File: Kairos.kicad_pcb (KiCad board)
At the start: 2 copper layers, 285 x 94.6 mm, 134 parts, among them Q1 NSS40301MZ4T1G, SW1 SW_RST1, U1 ATMEGA32U2-AU, Y1 Crystal_GND24

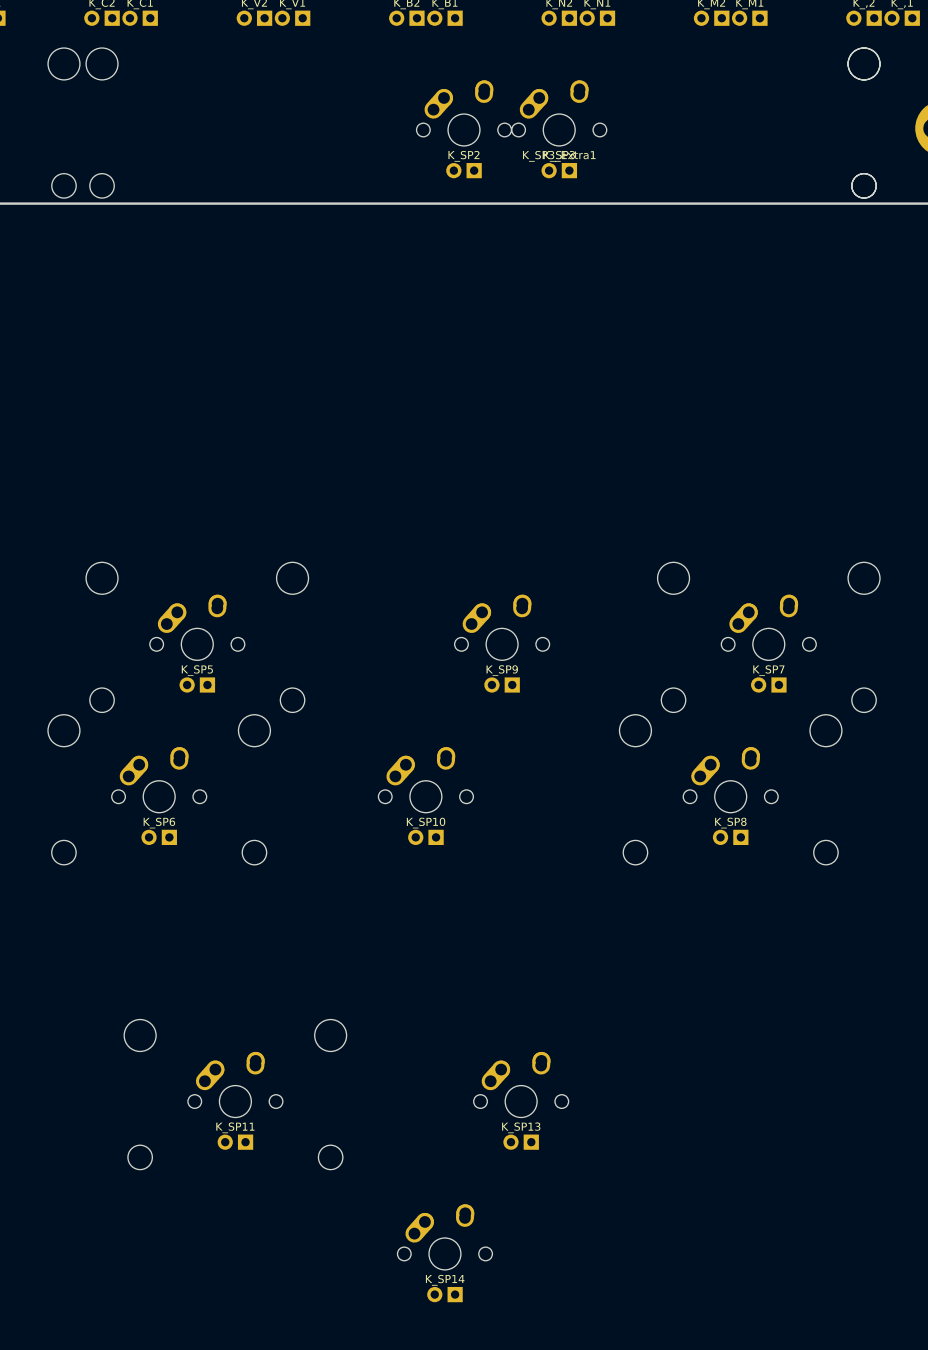
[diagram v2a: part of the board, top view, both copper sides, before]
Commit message: Remove SP14, clean up PCB
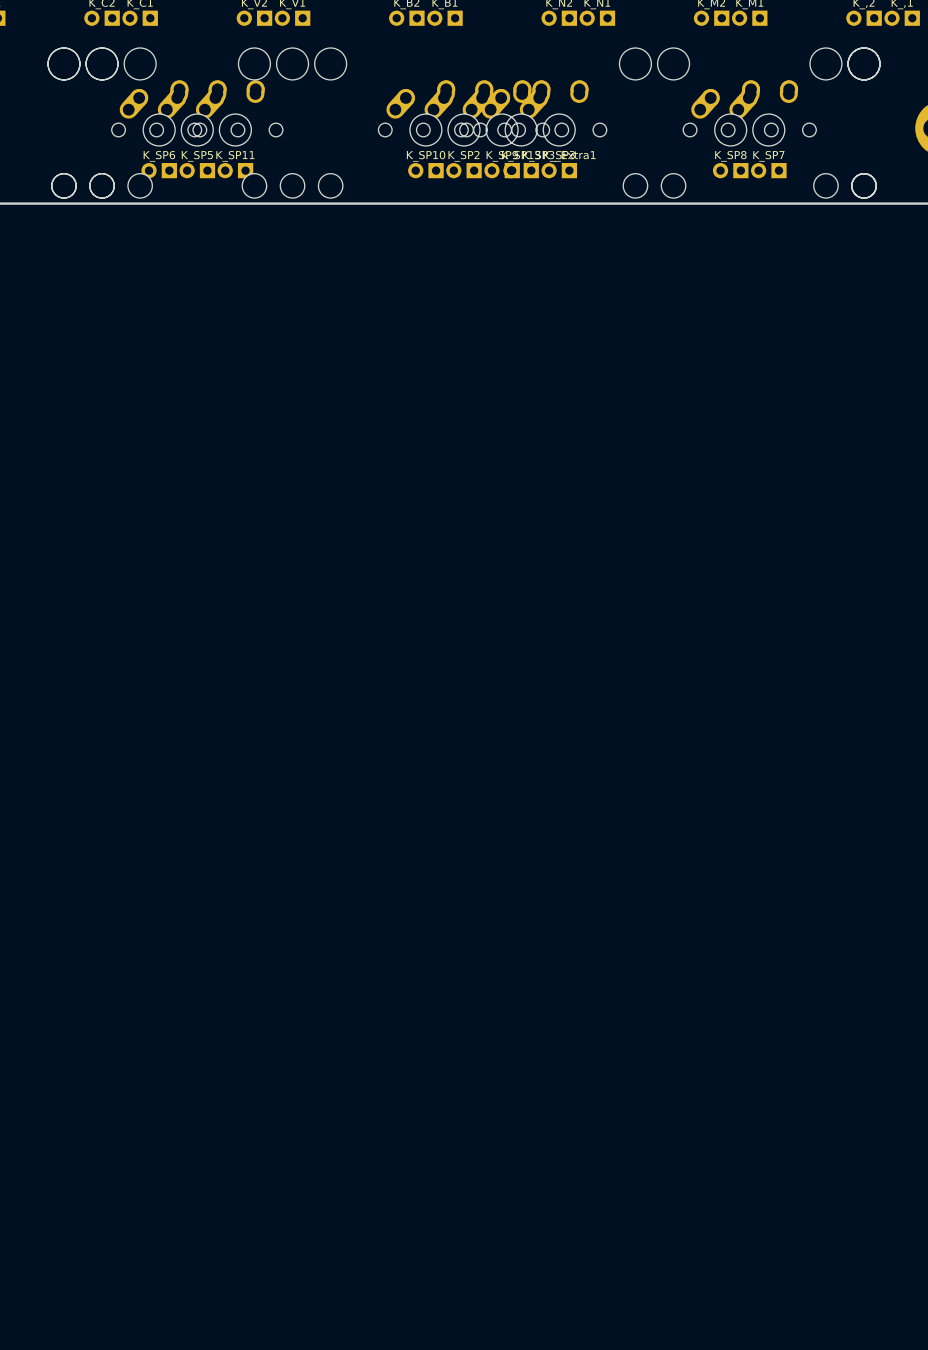
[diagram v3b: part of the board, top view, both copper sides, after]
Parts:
- removed K_SP14: MX-1U, MX_Alps_Hybrid:MX-1U
- moved K_SP11 121.4 mm to (107.2, 107.2)
- moved K_SP13 121.4 mm to (142.9, 107.2)
- moved K_SP10 83.3 mm to (131.0, 107.2)
- moved K_SP6 83.3 mm to (97.6, 107.2)
- moved K_SP8 83.3 mm to (169.1, 107.2)
- moved K_SP5 64.3 mm to (102.4, 107.2)
- moved K_SP7 64.3 mm to (173.8, 107.2)
- moved K_SP9 64.3 mm to (140.5, 107.2)
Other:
- board text removed: "Addons to RM7 and RM12"
- board text removed: "Split 6 Combined with 2.75 from Var2, Shares 2.75 from Var1 for 2.25"
- board text removed: "Split 6 Combined with Split 6.25 Var1"
- board text removed: "Split 6.25 Variant 1"
- board text removed: "Split 6.25 Variant 2"
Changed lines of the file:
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@@
 (kicad_pcb (version 4) (host pcbnew 4.0.6)
   (general
-    (links 573)
-    (no_connects 307)
+    (links 567)
+    (no_connects 303)
     (area 0 0 0 0)
     (thickness 1.6)
-    (drawings 7)
+    (drawings 2)
     (tracks 278)
     (zones 0)
-    (modules 134)
+    (modules 133)
     (nets 189)
   )
@@
   )
   (module MX_Alps_Hybrid:MX-1.25U (layer F.Cu)
-    (at 140.49375 171.45)
+    (at 140.49375 107.15625)
     (fp_text reference K_SP9 (at 0 3.175) (layer F.SilkS)
       (effects (font (size 1 1) (thickness 0.15)))
@@
   )
   (module MX_Alps_Hybrid:MX-1.25U (layer F.Cu)
-    (at 130.96875 190.5)
+    (at 130.96875 107.15625)
     (fp_text reference K_SP10 (at 0 3.175) (layer F.SilkS)
       (effects (font (size 1 1) (thickness 0.15)))
@@
   )
   (module MX_Alps_Hybrid:MX-1U (layer F.Cu)
-    (at 133.35 247.65)
-    (fp_text reference K_SP14 (at 0 3.175) (layer F.SilkS)
-      (effects (font (size 1 1) (thickness 0.15)))
-    )
-    (fp_text value MX-1U (at 0 -7.9375) (layer Dwgs.User)
-      (effects (font (size 1 1) (thickness 0.15)))
-    )
-    (fp_line (start 5 -7) (end 7 -7) (layer Dwgs.User) (width 0.15))
-    (fp_line (start 7 -7) (end 7 -5) (layer Dwgs.User) (width 0.15))
-    (fp_line (start 5 7) (end 7 7) (layer Dwgs.User) (width 0.15))
-    (fp_line (start 7 7) (end 7 5) (layer Dwgs.User) (width 0.15))
-    (fp_line (start -7 5) (end -7 7) (layer Dwgs.User) (width 0.15))
-    (fp_line (start -7 7) (end -5 7) (layer Dwgs.User) (width 0.15))
-    (fp_line (start -5 -7) (end -7 -7) (layer Dwgs.User) (width 0.15))
-    (fp_line (start -7 -7) (end -7 -5) (layer Dwgs.User) (width 0.15))
-    (fp_line (start -9.525 -9.525) (end 9.525 -9.525) (layer Dwgs.User) (width 0.15))
-    (fp_line (start 9.525 -9.525) (end 9.525 9.525) (layer Dwgs.User) (width 0.15))
-    (fp_line (start 9.525 9.525) (end -9.525 9.525) (layer Dwgs.User) (width 0.15))
-    (fp_line (start -9.525 9.525) (end -9.525 -9.525) (layer Dwgs.User) (width 0.15))
-    (pad 2 thru_hole oval (at 2.5 -4.5 86.0548) (size 2.831378 2.25) (drill 1.47 (offset 0.290689 0)) (layers *.Cu *.Mask)
-      (net 74 COL4))
-    (pad 2 thru_hole circle (at 2.54 -5.08) (size 2.25 2.25) (drill 1.47) (layers *.Cu *.Mask)
-      (net 74 COL4))
-    (pad 1 thru_hole oval (at -3.81 -2.54 48.09963212) (size 4.211556 2.25) (drill 1.47 (offset 0.980778 0)) (layers *.Cu *.Mask)
-      (net 35 ROW8))
-    (pad "" np_thru_hole circle (at 0 0) (size 3.9878 3.9878) (drill 3.9878) (layers *.Cu *.Mask))
-    (pad 1 thru_hole circle (at -2.5 -4) (size 2.25 2.25) (drill 1.47) (layers *.Cu *.Mask)
-      (net 35 ROW8))
-    (pad 3 thru_hole circle (at -1.27 5.08) (size 1.905 1.905) (drill 1.04) (layers *.Cu *.Mask)
-      (net 187 "Net-(K_SP10-Pad3)"))
-    (pad 4 thru_hole rect (at 1.27 5.08) (size 1.905 1.905) (drill 1.04) (layers *.Cu *.Mask)
-      (net 2 LEDGND))
-    (pad "" np_thru_hole circle (at -5.08 0 48.0996) (size 1.7018 1.7018) (drill 1.7018) (layers *.Cu *.Mask))
-    (pad "" np_thru_hole circle (at 5.08 0 48.0996) (size 1.7018 1.7018) (drill 1.7018) (layers *.Cu *.Mask))
-  )
-  (module MX_Alps_Hybrid:MX-1U (layer F.Cu)
-    (at 142.875 228.6)
+    (at 142.875 107.15625)
     (fp_text reference K_SP13 (at 0 3.175) (layer F.SilkS)
       (effects (font (size 1 1) (thickness 0.15)))
@@
   )
   (module MX_Alps_Hybrid:MX-2.75U-ReversedStabilizer (layer F.Cu)
-    (at 102.39375 171.45)
+    (at 102.39375 107.15625)
     (fp_text reference K_SP5 (at 0 3.175) (layer F.SilkS)
       (effects (font (size 1 1) (thickness 0.15)))
@@
   )
   (module MX_Alps_Hybrid:MX-2.25U-ReversedStabilizer (layer F.Cu)
-    (at 97.63125 190.5)
+    (at 97.63125 107.15625)
     (fp_text reference K_SP6 (at 0 3.175) (layer F.SilkS)
       (effects (font (size 1 1) (thickness 0.15)))
@@
   )
   (module MX_Alps_Hybrid:MX-2.25U-ReversedStabilizer (layer F.Cu)
-    (at 173.83125 171.45)
+    (at 173.83125 107.15625)
     (fp_text reference K_SP7 (at 0 3.175) (layer F.SilkS)
       (effects (font (size 1 1) (thickness 0.15)))
@@
   )
   (module MX_Alps_Hybrid:MX-2.75U-ReversedStabilizer (layer F.Cu)
-    (at 169.06875 190.5)
+    (at 169.06875 107.15625)
     (fp_text reference K_SP8 (at 0 3.175) (layer F.SilkS)
       (effects (font (size 1 1) (thickness 0.15)))
@@
   )
   (module MX_Alps_Hybrid:MX-2.75U-ReversedStabilizer (layer F.Cu)
-    (at 107.15625 228.6)
+    (at 107.15625 107.15625)
     (fp_text reference K_SP11 (at 0 3.175) (layer F.SilkS)
       (effects (font (size 1 1) (thickness 0.15)))
@@
     (pad "" np_thru_hole circle (at 11.90625 -8.255) (size 3.9878 3.9878) (drill 3.9878) (layers *.Cu *.Mask))
   )
-  (gr_text "To left and right:\n1.5-1.25-1.5 setups for\napple row (6.5U Space shares SP3)\n" (at 143.66875 285.75) (layer Dwgs.User)
-    (effects (font (size 1.5 1.5) (thickness 0.3)))
-  )
-  (gr_text "Addons to\nRM7 and RM12" (at 256.38125 246.85625) (layer Dwgs.User)
-    (effects (font (size 1.5 1.5) (thickness 0.3)))
-  )
-  (gr_text "Split 6\nCombined with 2.75 from Var2,\nShares 2.75 from Var1 for 2.25\n" (at 164.30625 246.85625) (layer Dwgs.User)
-    (effects (font (size 1.5 1.5) (thickness 0.3)))
-  )
-  (gr_text "Split 6\nCombined with\nSplit 6.25 Var1" (at 162.71875 228.6) (layer Dwgs.User)
-    (effects (font (size 1.5 1.5) (thickness 0.3)))
-  )
-  (gr_text "Split 6.25\nVariant 2\n" (at 204.7875 190.5) (layer Dwgs.User)
-    (effects (font (size 1.5 1.5) (thickness 0.3)))
-  )
-  (gr_text "Split 6.25\nVariant 1" (at 204.7875 170.65625) (layer Dwgs.User)
+  (gr_text 107.15625 (at 237.33125 150.8125) (layer Dwgs.User)
     (effects (font (size 1.5 1.5) (thickness 0.3)))
   )
-  (gr_text 107.15625 (at 237.33125 150.8125) (layer Dwgs.User)
+  (gr_text "To left and right:\n1.5-1.25-1.5 setups for\napple row (6.5U Space shares SP3)\n" (at 143.66875 285.75) (layer Dwgs.User)
     (effects (font (size 1.5 1.5) (thickness 0.3)))
   )

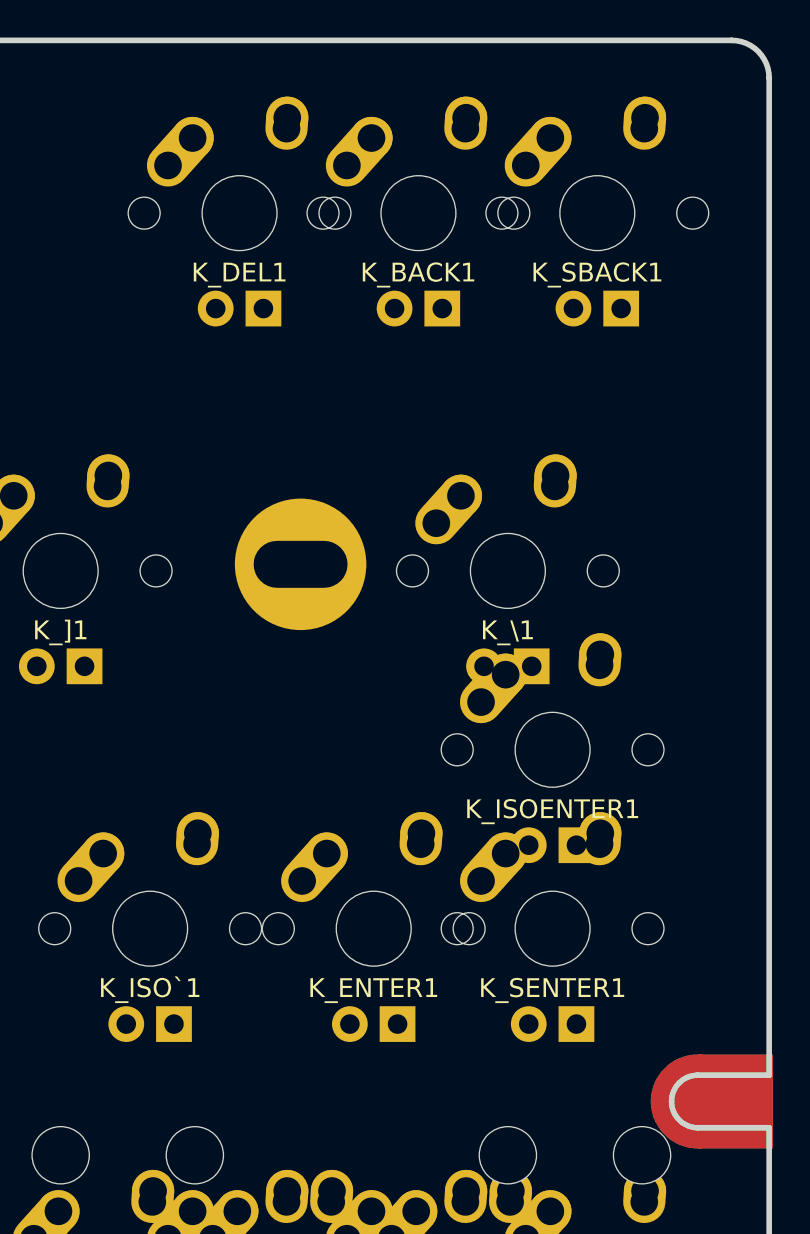
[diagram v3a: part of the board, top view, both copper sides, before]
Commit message: Fix first batch of wrong size footprints
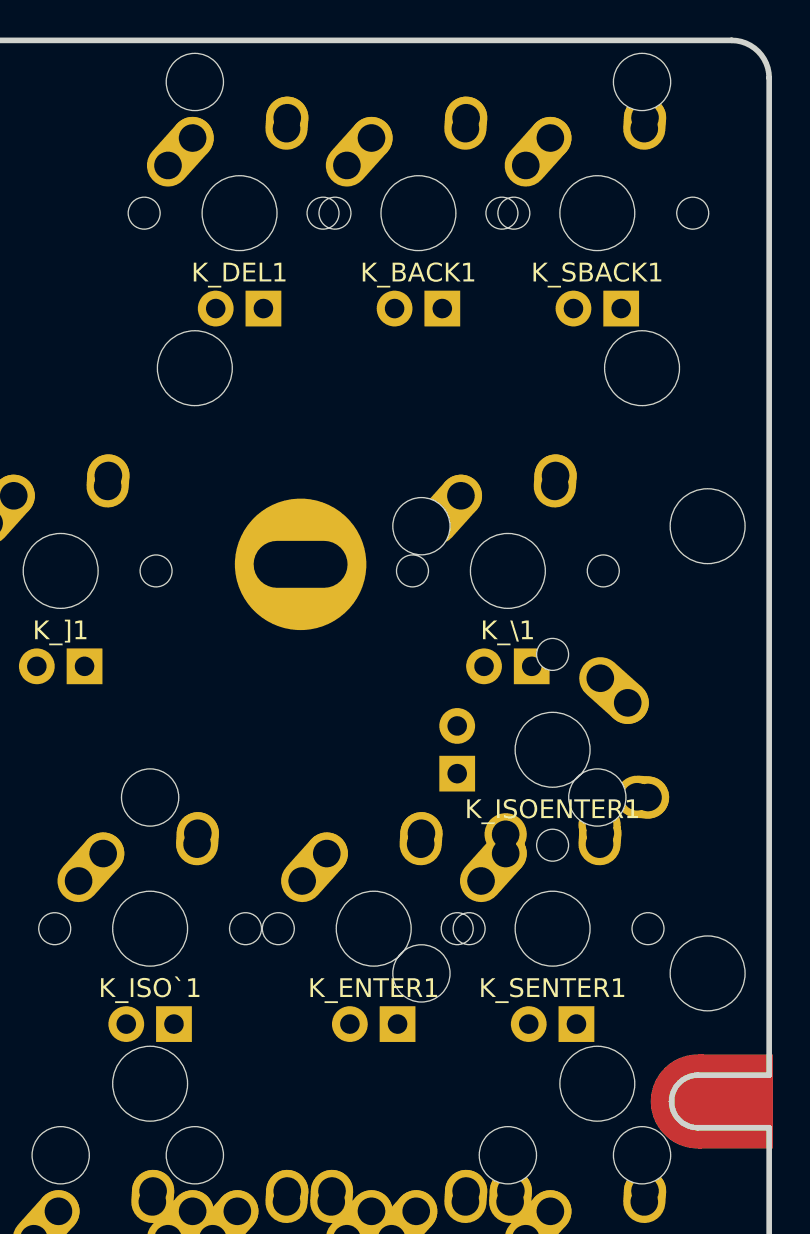
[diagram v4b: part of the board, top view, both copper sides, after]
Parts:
- K_BACK1: footprint MX_Alps_Hybrid:MX-1U -> MX_Alps_Hybrid:MX-2U
- K_CAPS1: footprint MX_Alps_Hybrid:MX-1U -> MX_Alps_Hybrid:MX-1.75U
- K_CAPS2: footprint MX_Alps_Hybrid:MX-1U -> MX_Alps_Hybrid:MX-1.25U
- K_ENTER1: footprint MX_Alps_Hybrid:MX-1U -> MX_Alps_Hybrid:MX-2.25U
- K_ISOENTER1: footprint MX_Alps_Hybrid:MX-1U -> MX_Alps_Hybrid:MX-ISO-Combined
